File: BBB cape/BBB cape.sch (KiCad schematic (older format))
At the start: 7 parts, among them P9 BeagleBone_Black_Header

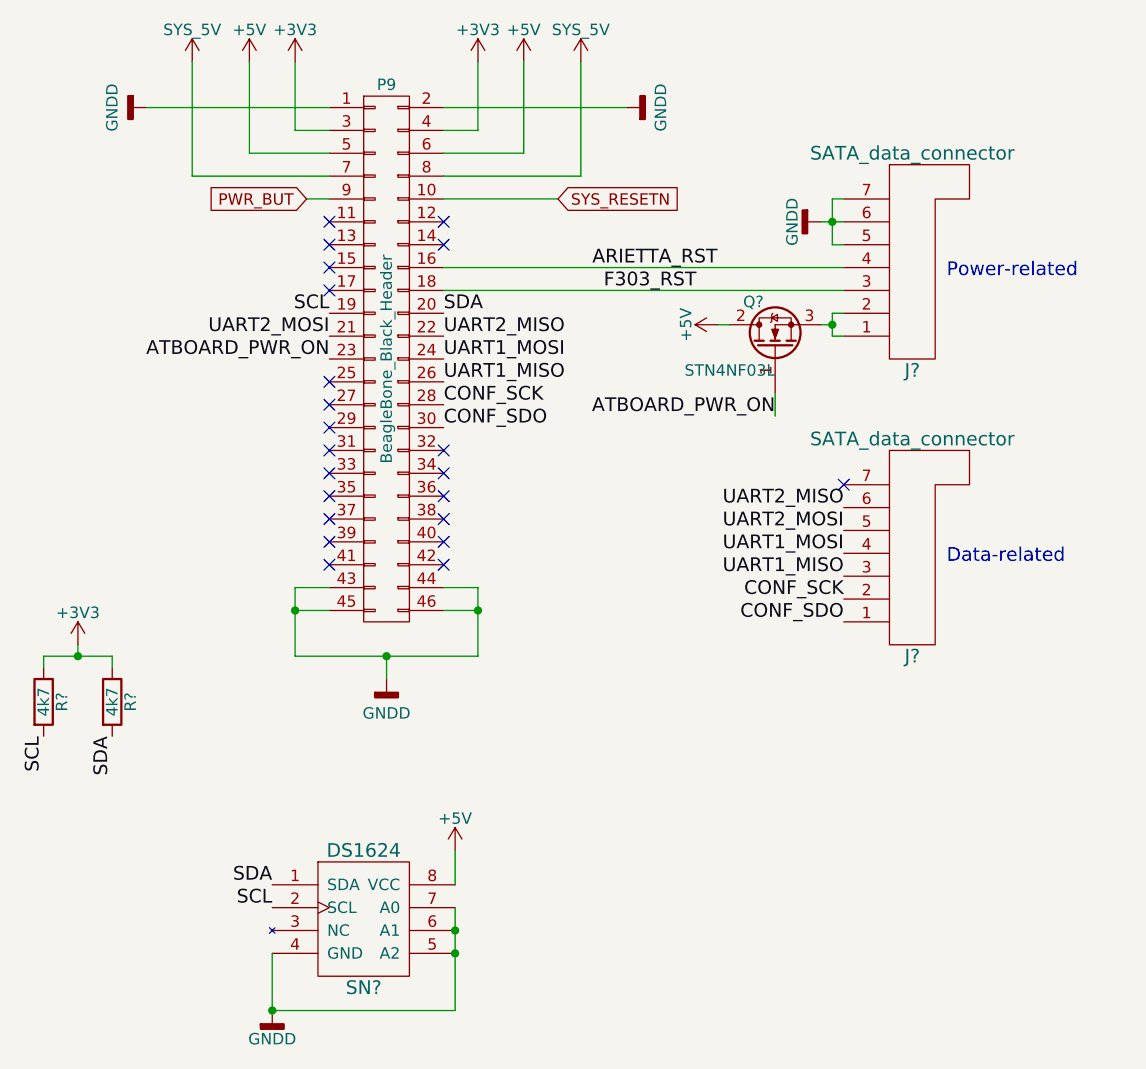
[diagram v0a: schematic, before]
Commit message: Finished adding components and mapping connections for BBB cape
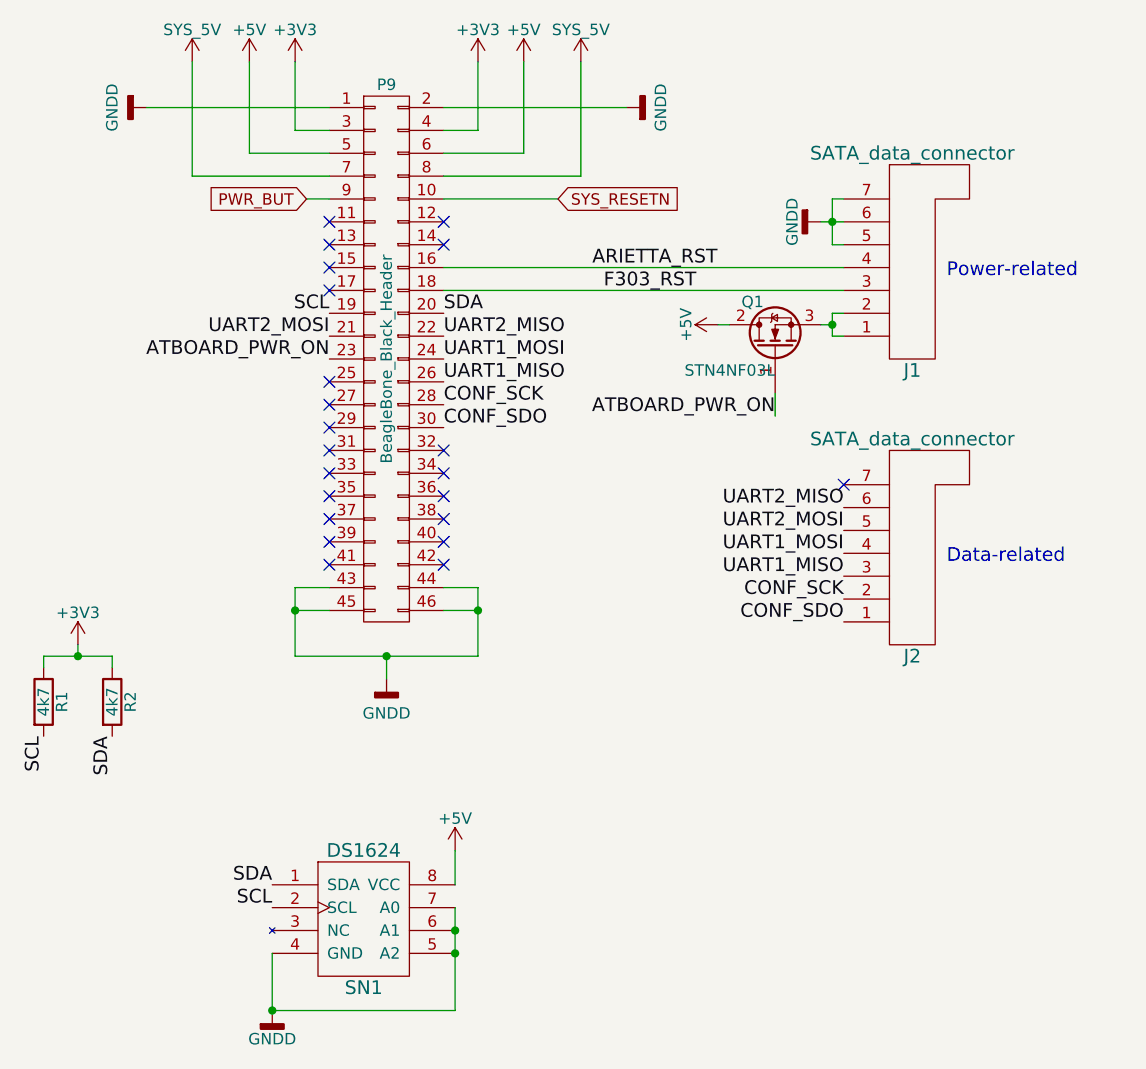
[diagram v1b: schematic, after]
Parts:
- gave numbers to parts that had none: 6
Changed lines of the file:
@@
 $EndDescr
 $Comp
-L GNDD #PWR01
+L GNDD #PWR7
 U 1 1 5589785A
 P 2450 3650
-F 0 "#PWR01" H 2450 3400 50  0001 C CNN
+F 0 "#PWR7" H 2450 3400 50  0001 C CNN
 F 1 "GNDD" H 2450 3500 50  0000 C CNN
 F 2 "" H 2450 3650 60  0000 C CNN
@@
 Connection ~ 2450 3550
 $Comp
-L GNDD #PWR02
+L GNDD #PWR12
 U 1 1 558978D3
 P 3500 1150
-F 0 "#PWR02" H 3500 900 50  0001 C CNN
+F 0 "#PWR12" H 3500 900 50  0001 C CNN
 F 1 "GNDD" H 3500 1000 50  0000 C CNN
 F 2 "" H 3500 1150 60  0000 C CNN
@@
 $EndComp
 $Comp
-L GNDD #PWR03
+L GNDD #PWR2
 U 1 1 5589790A
 P 1400 1150
-F 0 "#PWR03" H 1400 900 50  0001 C CNN
+F 0 "#PWR2" H 1400 900 50  0001 C CNN
 F 1 "GNDD" H 1400 1000 50  0000 C CNN
 F 2 "" H 1400 1150 60  0000 C CNN
@@
 $EndComp
 $Comp
-L +3V3 #PWR06
+L +3V3 #PWR9
 U 1 1 55897A67
 P 2850 950
-F 0 "#PWR06" H 2850 800 50  0001 C CNN
+F 0 "#PWR9" H 2850 800 50  0001 C CNN
 F 1 "+3V3" H 2850 1090 50  0000 C CNN
 F 2 "" H 2850 950 60  0000 C CNN
@@
 $EndComp
 $Comp
-L +5V #PWR07
+L +5V #PWR10
 U 1 1 55897A7F
 P 3050 950
-F 0 "#PWR07" H 3050 800 50  0001 C CNN
+F 0 "#PWR10" H 3050 800 50  0001 C CNN
 F 1 "+5V" H 3050 1090 50  0000 C CNN
 F 2 "" H 3050 950 60  0000 C CNN
@@
 	3300 1450 2700 1450
 $Comp
-L +3V3 #PWR08
+L +3V3 #PWR6
 U 1 1 55897EE7
 P 2050 950
-F 0 "#PWR08" H 2050 800 50  0001 C CNN
+F 0 "#PWR6" H 2050 800 50  0001 C CNN
 F 1 "+3V3" H 2050 1090 50  0000 C CNN
 F 2 "" H 2050 950 60  0000 C CNN
@@
 $EndComp
 $Comp
-L +5V #PWR09
+L +5V #PWR4
 U 1 1 55897EF8
 P 1850 950
-F 0 "#PWR09" H 1850 800 50  0001 C CNN
+F 0 "#PWR4" H 1850 800 50  0001 C CNN
 F 1 "+5V" H 1850 1090 50  0000 C CNN
 F 2 "" H 1850 950 60  0000 C CNN
@@
 	2200 1150 1400 1150
 $Comp
-L SYS_5V #PWR010
+L SYS_5V #PWR11
 U 1 1 55898497
 P 3300 950
-F 0 "#PWR010" H 3300 800 50  0001 C CNN
+F 0 "#PWR11" H 3300 800 50  0001 C CNN
 F 1 "SYS_5V" H 3300 1090 50  0000 C CNN
 F 2 "" H 3300 950 60  0000 C CNN
@@
 $EndComp
 $Comp
-L SYS_5V #PWR011
+L SYS_5V #PWR3
 U 1 1 558984AF
 P 1600 950
-F 0 "#PWR011" H 1600 800 50  0001 C CNN
+F 0 "#PWR3" H 1600 800 50  0001 C CNN
 F 1 "SYS_5V" H 1600 1090 50  0000 C CNN
 F 2 "" H 1600 950 60  0000 C CNN
@@
 F303_RST
 $Comp
-L SATA_data_connector J?
+L SATA_data_connector J1
 U 1 1 5A160A2B
 P 4750 1850
-F 0 "J?" H 4750 1400 60  0000 C CNN
+F 0 "J1" H 4750 1400 60  0000 C CNN
 F 1 "SATA_data_connector" H 4750 2350 60  0000 C CNN
 F 2 "" H 4750 1850 60  0001 C CNN
@@
 $EndComp
 $Comp
-L SATA_data_connector J?
+L SATA_data_connector J2
 U 1 1 5A160A78
 P 4750 3100
-F 0 "J?" H 4750 2650 60  0000 C CNN
+F 0 "J2" H 4750 2650 60  0000 C CNN
 F 1 "SATA_data_connector" H 4750 3600 60  0000 C CNN
 F 2 "" H 4750 3100 60  0001 C CNN
@@
 Data-related
 $Comp
-L GNDD #PWR?
+L GNDD #PWR14
 U 1 1 5A160B35
 P 4350 1650
-F 0 "#PWR?" H 4350 1400 50  0001 C CNN
+F 0 "#PWR14" H 4350 1400 50  0001 C CNN
 F 1 "GNDD" H 4350 1525 50  0000 C CNN
 F 2 "" H 4350 1650 50  0001 C CNN
@@
 	4400 2150 4450 2150
 $Comp
-L +5V #PWR?
+L +5V #PWR13
 U 1 1 5A160BFF
 P 3900 2100
-F 0 "#PWR?" H 3900 1950 50  0001 C CNN
+F 0 "#PWR13" H 3900 1950 50  0001 C CNN
 F 1 "+5V" H 3900 2240 50  0000 C CNN
 F 2 "" H 3900 2100 50  0001 C CNN
@@
 NoConn ~ 2700 1650
 $Comp
-L DS1624 SN?
+L DS1624 SN1
 U 1 1 5A161F75
 P 2350 4700
-F 0 "SN?" H 2350 4400 60  0000 C CNN
+F 0 "SN1" H 2350 4400 60  0000 C CNN
 F 1 "DS1624" H 2350 5000 60  0000 C CNN
 F 2 "" H 2350 4700 60  0001 C CNN
@@
 $EndComp
 $Comp
-L Q_NMOS_GDS Q?
+L Q_NMOS_GDS Q1
 U 1 1 5A163BA9
 P 4150 2200
-F 0 "Q?" V 4350 2250 50  0000 L CNN
+F 0 "Q1" V 4350 2250 50  0000 L CNN
 F 1 "STN4NF03L " V 4050 2200 50  0000 L CNN
 F 2 "" H 4350 2300 50  0001 C CNN
@@
 SCL
 $Comp
-L GNDD #PWR?
+L GNDD #PWR5
 U 1 1 5A164072
 P 1950 5100
-F 0 "#PWR?" H 1950 4850 50  0001 C CNN
+F 0 "#PWR5" H 1950 4850 50  0001 C CNN
 F 1 "GNDD" H 1950 4975 50  0000 C CNN
 F 2 "" H 1950 5100 50  0001 C CNN
@@
 	1950 5100 1950 4850
 $Comp
-L +5V #PWR?
+L +5V #PWR8
 U 1 1 5A1640C0
 P 2750 4400
-F 0 "#PWR?" H 2750 4250 50  0001 C CNN
+F 0 "#PWR8" H 2750 4250 50  0001 C CNN
 F 1 "+5V" H 2750 4540 50  0000 C CNN
 F 2 "" H 2750 4400 50  0001 C CNN
@@
 Connection ~ 1950 5100
 $Comp
-L R R?
+L R R1
 U 1 1 5A164288
 P 950 3750
-F 0 "R?" V 1030 3750 50  0000 C CNN
+F 0 "R1" V 1030 3750 50  0000 C CNN
 F 1 "4k7" V 950 3750 50  0000 C CNN
 F 2 "" V 880 3750 50  0001 C CNN
@@
 $EndComp
 $Comp
-L R R?
+L R R2
 U 1 1 5A1642BF
 P 1250 3750
-F 0 "R?" V 1330 3750 50  0000 C CNN
+F 0 "R2" V 1330 3750 50  0000 C CNN
 F 1 "4k7" V 1250 3750 50  0000 C CNN
 F 2 "" V 1180 3750 50  0001 C CNN
@@
 $EndComp
 $Comp
-L +3V3 #PWR?
+L +3V3 #PWR1
 U 1 1 5A1643F6
 P 1100 3500
-F 0 "#PWR?" H 1100 3350 50  0001 C CNN
+F 0 "#PWR1" H 1100 3350 50  0001 C CNN
 F 1 "+3V3" H 1100 3640 50  0000 C CNN
 F 2 "" H 1100 3500 50  0001 C CNN

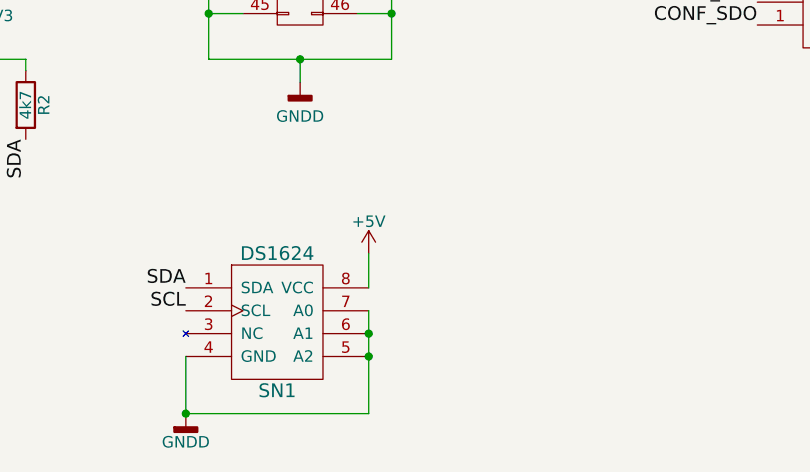
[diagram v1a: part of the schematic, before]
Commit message: Assigned some components
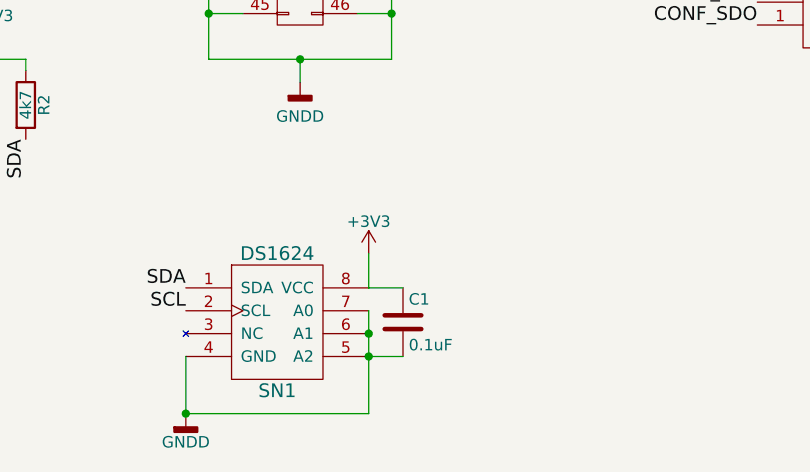
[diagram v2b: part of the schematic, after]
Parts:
- added C1: 0.1uF, Resistors_SMD:R_0805_HandSoldering, symbol C
- R1, R2: footprint (none) -> Resistors_SMD:R_0805_HandSoldering
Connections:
- net +3V3: now also SN1.8 (VCC), C1.1
- net +5V: no longer SN1.8 (VCC)
- net GNDD: now also C1.2
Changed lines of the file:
@@
 Wire Wire Line
 	1950 5100 1950 4850
-$Comp
-L +5V #PWR8
-U 1 1 5A1640C0
-P 2750 4400
-F 0 "#PWR8" H 2750 4250 50  0001 C CNN
-F 1 "+5V" H 2750 4540 50  0000 C CNN
-F 2 "" H 2750 4400 50  0001 C CNN
-F 3 "" H 2750 4400 50  0001 C CNN
-	1    2750 4400
-	1    0    0    -1
-$EndComp
 Wire Wire Line
 	2750 4400 2750 4550
@@
 F 0 "R1" V 1030 3750 50  0000 C CNN
 F 1 "4k7" V 950 3750 50  0000 C CNN
-F 2 "" V 880 3750 50  0001 C CNN
+F 2 "Resistors_SMD:R_0805_HandSoldering" V 880 3750 50  0001 C CNN
 F 3 "" H 950 3750 50  0001 C CNN
 	1    950  3750
@@
 F 0 "R2" V 1330 3750 50  0000 C CNN
 F 1 "4k7" V 1250 3750 50  0000 C CNN
-F 2 "" V 1180 3750 50  0001 C CNN
+F 2 "Resistors_SMD:R_0805_HandSoldering" V 1180 3750 50  0001 C CNN
 F 3 "" H 1250 3750 50  0001 C CNN
 	1    1250 3750
@@
 Text Label 1250 3900 3    60   ~ 0
 SDA
+$Comp
+L +3V3 #PWR8
+U 1 1 5A189CA6
+P 2750 4400
+F 0 "#PWR8" H 2750 4250 50  0001 C CNN
+F 1 "+3V3" H 2750 4540 50  0000 C CNN
+F 2 "" H 2750 4400 50  0001 C CNN
+F 3 "" H 2750 4400 50  0001 C CNN
+	1    2750 4400
+	1    0    0    -1
+$EndComp
+$Comp
+L C C1
+U 1 1 5A189DB0
+P 2900 4700
+F 0 "C1" H 2925 4800 50  0000 L CNN
+F 1 "0.1uF" H 2925 4600 50  0000 L CNN
+F 2 "Resistors_SMD:R_0805_HandSoldering" H 2938 4550 50  0001 C CNN
+F 3 "" H 2900 4700 50  0001 C CNN
+	1    2900 4700
+	1    0    0    -1
+$EndComp
+Wire Wire Line
+	2750 4550 2900 4550
+Wire Wire Line
+	2900 4850 2750 4850
 $EndSCHEMATC
